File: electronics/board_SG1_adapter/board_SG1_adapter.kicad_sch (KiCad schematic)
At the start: 2 parts

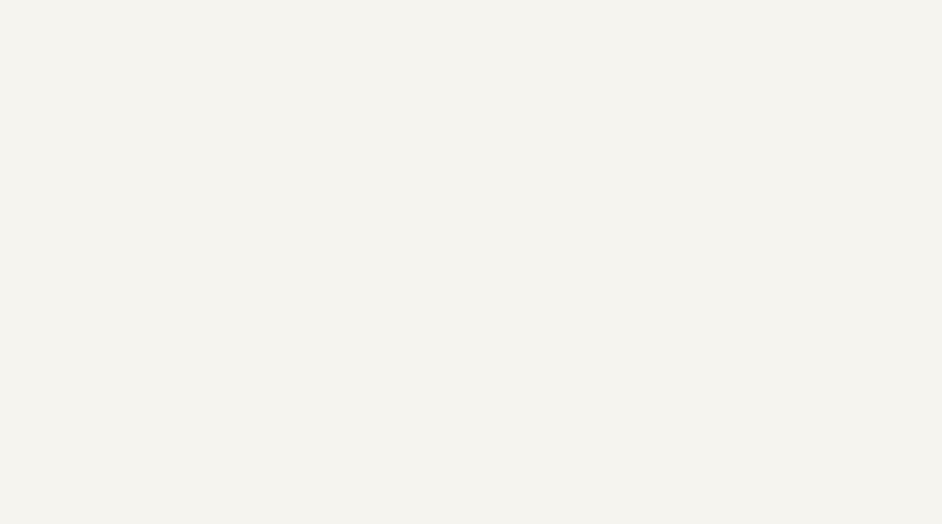
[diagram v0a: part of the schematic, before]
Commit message: WIP schematic entry and component+footprint definitions
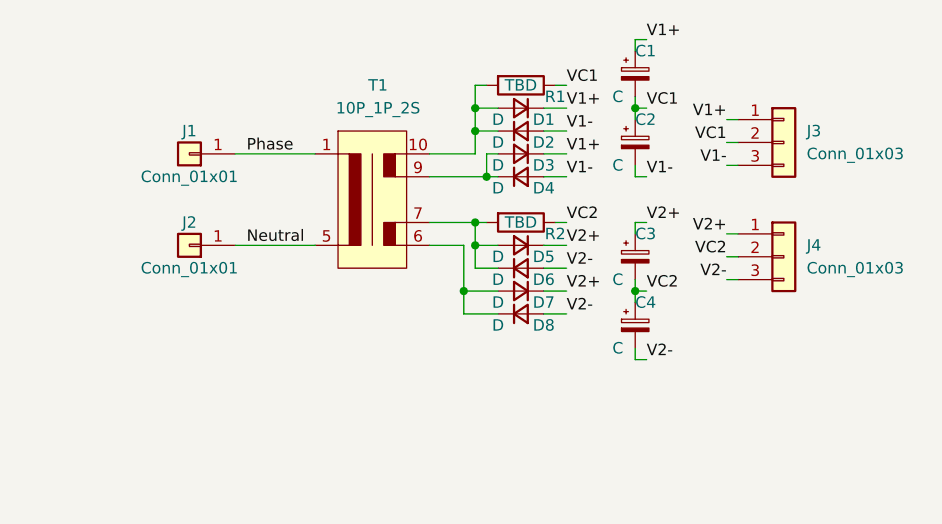
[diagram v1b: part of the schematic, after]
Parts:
- added C1, C2, C3, C4: C, symbol Device:C_Polarized_Small
- added D1, D2, D3, D4, D5, D6, D7, D8: D, Diode_SMD:D_SMA, symbol Device:D_Small
- added J1, J2: Conn_01x01, SquantorConnectors:pad_power, symbol Connector_Generic:Conn_01x01
- added J3, J4: Conn_01x03, symbol Connector_Generic:Conn_01x03
- added R1, R2: TBD, SquantorRcl:R_1206, symbol Device:R
- added T1: 10P_1P_2S, symbol SquantorTransformer:10P_1P_2S
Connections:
- new net: D3.2 (A), D4.1 (K), T1.9
- new net: D5.2 (A), D6.1 (K), R2.2, T1.7
- new net: D1.2 (A), D2.1 (K), R1.2, T1.10
- new net: D7.2 (A), D8.1 (K), T1.6
- new net Neutral: J2.1 (Pin_1), T1.5
- new net Phase: J1.1 (Pin_1), T1.1
- new net V1+: C1.1, D1.1 (K), D3.1 (K), J3.1 (Pin_1)
- new net V1-: C2.2, D2.2 (A), D4.2 (A), J3.3 (Pin_3)
- new net V2+: C3.1, D5.1 (K), D7.1 (K), J4.1 (Pin_1)
- new net V2-: C4.2, D6.2 (A), D8.2 (A), J4.3 (Pin_3)
- new net VC1: C1.2, C2.1, J3.2 (Pin_2), R1.1
- new net VC2: C3.2, C4.1, J4.2 (Pin_2), R2.1

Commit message: WIP rectifier section
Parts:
- added R3, R4: TBD, SquantorRcl:R_1206, symbol Device:R
- D1, D2, D3, D4, D5, D6, D7, D8: footprint Diode_SMD:D_SMA -> Diode_SMD:D_SMB
- T1: footprint (none) -> SquantorTransformer:10pin_5pitch_32x27_1Pri_2Sec
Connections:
- net VC1: now also R2.1
- net VC2: now also R3.1, R4.1; no longer R2.1
- net P1B: now reaches D3.2 (A), D4.1 (K), T1.9
- net P1B: now also R2.2
- net P2A: now reaches D5.2 (A), D6.1 (K), T1.7
- net P2A: now also R3.2; no longer R2.2
- net P1A: now reaches D1.2 (A), D2.1 (K), R1.2, T1.10
- net P2B: now reaches D7.2 (A), D8.1 (K), T1.6
- net P2B: now also R4.2
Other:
- moved on the sheet: D1, D2, D7, D8, R1, R2

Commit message: WIP placing and selecting components
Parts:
- added C5, C6: 100n, SquantorRcl:C_0805+0603, symbol Device:C_Small
- C1, C2, C3, C4: footprint (none) -> SquantorRcl:C-050-075-100-elco
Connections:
- net P2B: now also C5.1, C6.1
- net V2+: now also C5.2
- net V2-: now also C6.2
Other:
- moved on the sheet: D7, D8, R4

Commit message: WIP further development
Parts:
- removed J3, J4: Conn_01x03, symbol Connector_Generic:Conn_01x03
- added C10, C11, C12, C7, C8, C9: 100n, SquantorRcl:C_0805+0603, symbol Device:C_Small
- added C13, C14, C15, C16, C17, C18, C19, C20, C21, C22, C23, C24, C25, C26: 10u, SquantorRcl:C_1206_0805, symbol Device:C_Small
- added J3: Conn_01x06, Connector_Molex:Molex_KK-254_AE-6410-06A_1x06_P2.54mm_Vertical, symbol Connector_Generic:Conn_01x06
- C1, C2, C3, C4: footprint SquantorRcl:C-050-075-100-elco -> SquantorRcl:C-050-100-elco
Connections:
- net P1A: now also C7.1, C8.1
- net P1B: now also C10.1, C9.1
- net P2A: now also C11.1, C12.1
- net V1+: now also C13.1, C17.1, C19.1, C21.1, C23.1, C7.2, C9.2, J3.1 (Pin_1)
- net V1-: now also C10.2, C14.2, C17.2, C19.2, C21.2, C23.2, C8.2, J3.3 (Pin_3)
- net V2+: now also C11.2, C15.1, C18.1, C20.1, C22.1, C24.1, C25.1, J3.4 (Pin_4)
- net V2-: now also C12.2, C16.2, C18.2, C20.2, C22.2, C24.2, C26.2, J3.6 (Pin_6)
- net VC1: now also C13.2, C14.1, J3.2 (Pin_2)
- net VC2: now also C15.2, C16.1, C25.2, C26.1, J3.5 (Pin_5)
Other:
- moved on the sheet: C1, C2, C3, C4, C5, C6, D1, D2, D3, D4, D5, D6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

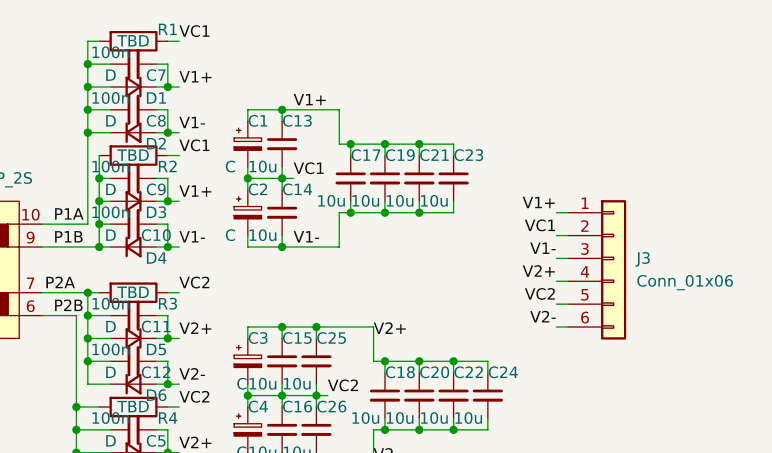
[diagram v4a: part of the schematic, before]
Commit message: routing completed WIP silk placement
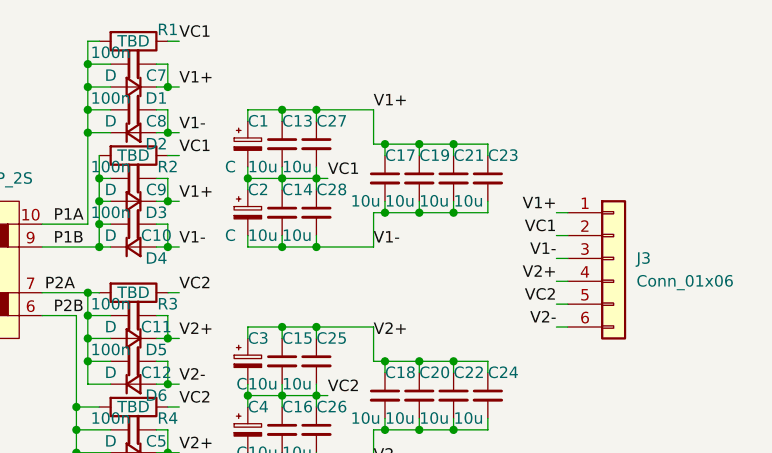
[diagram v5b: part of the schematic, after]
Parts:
- added C27, C28: 10u, SquantorRcl:C_1206_0805, symbol Device:C_Small
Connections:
- net V1+: now also C27.1
- net V1-: now also C28.2
- net VC1: now also C27.2, C28.1
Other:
- moved on the sheet: C17, C19, C21, C23

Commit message: silk placement completed
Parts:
- C1, C2, C3, C4: value C -> 100u
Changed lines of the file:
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@@
       (effects (font (size 1.27 1.27)) (justify left))
     )
-    (property "Value" "C" (id 1) (at 81.28 39.37 0)
+    (property "Value" "100u" (id 1) (at 78.74 39.37 0)
       (effects (font (size 1.27 1.27)) (justify left))
     )
@@
       (effects (font (size 1.27 1.27)) (justify left))
     )
-    (property "Value" "C" (id 1) (at 81.28 31.75 0)
+    (property "Value" "100u" (id 1) (at 78.74 31.75 0)
       (effects (font (size 1.27 1.27)) (justify left))
     )
@@
       (effects (font (size 1.27 1.27)) (justify left))
     )
-    (property "Value" "C" (id 1) (at 82.55 55.88 0)
+    (property "Value" "100u" (id 1) (at 78.74 55.88 0)
       (effects (font (size 1.27 1.27)) (justify left))
     )
@@
       (effects (font (size 1.27 1.27)) (justify left))
     )
-    (property "Value" "C" (id 1) (at 82.55 63.5 0)
+    (property "Value" "100u" (id 1) (at 78.74 63.5 0)
       (effects (font (size 1.27 1.27)) (justify left))
     )
@@
   (symbol_instances
     (path "/33a96a7d-b1b6-4d63-a112-8e0892e19753"
-      (reference "C1") (unit 1) (value "C") (footprint "SquantorRcl:C-050-100-elco")
+      (reference "C1") (unit 1) (value "100u") (footprint "SquantorRcl:C-050-100-elco")
     )
     (path "/2b78c5ce-aeac-4cdf-9dfa-5948914964b5"
-      (reference "C2") (unit 1) (value "C") (footprint "SquantorRcl:C-050-100-elco")
+      (reference "C2") (unit 1) (value "100u") (footprint "SquantorRcl:C-050-100-elco")
     )
     (path "/6118800c-273b-49bc-ae5c-e88a0e55130d"
-      (reference "C3") (unit 1) (value "C") (footprint "SquantorRcl:C-050-100-elco")
+      (reference "C3") (unit 1) (value "100u") (footprint "SquantorRcl:C-050-100-elco")
     )
     (path "/78f42d71-b71d-46fc-9742-f3a159a96a0b"
-      (reference "C4") (unit 1) (value "C") (footprint "SquantorRcl:C-050-100-elco")
+      (reference "C4") (unit 1) (value "100u") (footprint "SquantorRcl:C-050-100-elco")
     )
     (path "/431a0f33-663b-4db5-8d23-d3860d969f31"

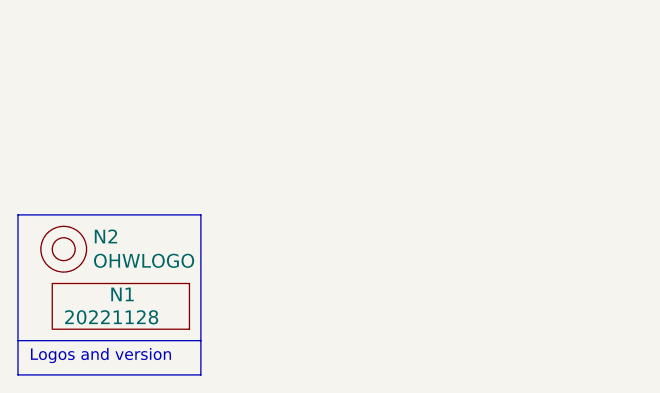
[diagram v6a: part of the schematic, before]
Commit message: added small fixes, through wire holes
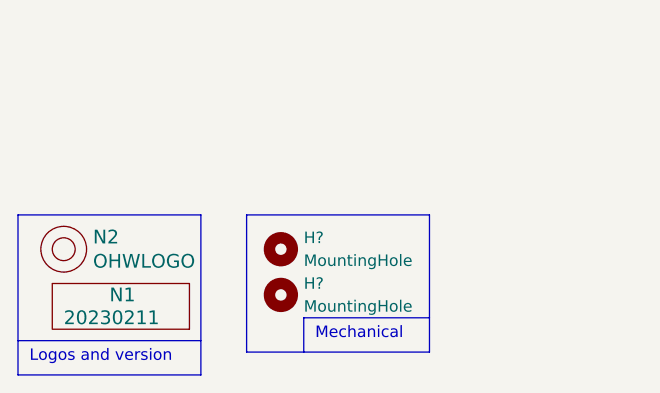
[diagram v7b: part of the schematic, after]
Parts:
- added H? (x2): MountingHole, MountingHole:MountingHole_2.2mm_M2, symbol Mechanical:MountingHole
- N1: value 20221128 -> 20230211
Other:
- note added: "Mechanical"
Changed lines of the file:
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@@
+    (stroke (width 0) (type default) (color 0 0 0 0))
+  )
+  (polyline (pts (xy 60.96 189.23) (xy 46.99 189.23))
     (stroke (width 0) (type default) (color 0 0 0 0))
   )
@@
     (stroke (width 0) (type default) (color 0 0 0 0))
   )
+  (polyline (pts (xy 46.99 189.23) (xy 46.99 193.04))
+    (stroke (width 0) (type default) (color 0 0 0 0))
+  )
   (wire (pts (xy 91.44 39.37) (xy 91.44 40.64))
     (stroke (width 0) (type default) (color 0 0 0 0))
@@
     (stroke (width 0) (type default) (color 0 0 0 0))
   )
+  (polyline (pts (xy 40.64 177.8) (xy 40.64 193.04))
+    (stroke (width 0) (type default) (color 0 0 0 0))
+  )
   (wire (pts (xy 106.68 60.96) (xy 102.87 60.96))
     (stroke (width 0) (type default) (color 0 0 0 0))
@@
     (stroke (width 0) (type default) (color 0 0 0 0))
   )
+  (polyline (pts (xy 60.96 193.04) (xy 60.96 177.8))
+    (stroke (width 0) (type default) (color 0 0 0 0))
+  )
   (wire (pts (xy 110.49 35.56) (xy 110.49 36.83))
     (stroke (width 0) (type default) (color 0 0 0 0))
@@
     (stroke (width 0) (type default) (color 0 0 0 0))
   )
+  (polyline (pts (xy 60.96 177.8) (xy 40.64 177.8))
+    (stroke (width 0) (type default) (color 0 0 0 0))
+  )
   (wire (pts (xy 73.66 20.32) (xy 74.93 20.32))
     (stroke (width 0) (type default) (color 0 0 0 0))
@@
     (stroke (width 0) (type default) (color 0 0 0 0))
   )
+  (polyline (pts (xy 40.64 193.04) (xy 60.96 193.04))
+    (stroke (width 0) (type default) (color 0 0 0 0))
+  )
   (wire (pts (xy 66.04 53.34) (xy 66.04 55.88))
     (stroke (width 0) (type default) (color 0 0 0 0))
@@
   )
   (text "Logos and version" (at 16.51 194.31 0)
+    (effects (font (size 1.27 1.27)) (justify left bottom))
+  )
+  (text "Mechanical" (at 48.26 191.77 0)
     (effects (font (size 1.27 1.27)) (justify left bottom))
   )
@@
       (effects (font (size 1.524 1.524)) (justify left))
     )
-    (property "Value" "20221128" (id 1) (at 20.32 189.23 0)
+    (property "Value" "20230211" (id 1) (at 20.32 189.23 0)
       (effects (font (size 1.524 1.524)) (justify left))
     )
@@
     (pin "2")
   )
+  (symbol (lib_id "Mechanical:MountingHole") (at 44.45 181.61 0) (unit 1)
+    (in_bom yes) (on_board yes) (fields_autoplaced)
+    (property "Reference" "H?" (id 0) (at 46.99 180.3399 0)
+      (effects (font (size 1.27 1.27)) (justify left))
+    )
+    (property "Value" "MountingHole" (id 1) (at 46.99 182.8799 0)
+      (effects (font (size 1.27 1.27)) (justify left))
+    )
+    (property "Footprint" "MountingHole:MountingHole_2.2mm_M2" (id 2) (at 44.45 181.61 0)
+      (effects (font (size 1.27 1.27)) hide)
+    )
+    (property "Datasheet" "~" (id 3) (at 44.45 181.61 0)
+      (effects (font (size 1.27 1.27)) hide)
+    )
+  )
   (symbol (lib_id "Connector_Generic:Conn_01x01") (at 34.29 48.26 180) (unit 1)
     (in_bom yes) (on_board yes)
@@
     (pin "2")
   )
+  (symbol (lib_id "Mechanical:MountingHole") (at 44.45 186.69 0) (unit 1)
+    (in_bom yes) (on_board yes) (fields_autoplaced)
+    (property "Reference" "H?" (id 0) (at 46.99 185.4199 0)
+      (effects (font (size 1.27 1.27)) (justify left))
+    )
+    (property "Value" "MountingHole" (id 1) (at 46.99 187.9599 0)
+      (effects (font (size 1.27 1.27)) (justify left))
+    )
+    (property "Footprint" "MountingHole:MountingHole_2.2mm_M2" (id 2) (at 44.45 186.69 0)
+      (effects (font (size 1.27 1.27)) hide)
+    )
+    (property "Datasheet" "~" (id 3) (at 44.45 186.69 0)
+      (effects (font (size 1.27 1.27)) hide)
+    )
+  )
   (symbol (lib_id "Device:D_Small") (at 71.12 63.5 180) (unit 1)
     (in_bom yes) (on_board yes)
@@
       (reference "D8") (unit 1) (value "D") (footprint "Diode_SMD:D_SMB")
     )
+    (path "/9a78483e-a4a9-442b-9b78-185e6ef8e163"
+      (reference "H?") (unit 1) (value "MountingHole") (footprint "MountingHole:MountingHole_2.2mm_M2")
+    )
+    (path "/c4c5520e-ab64-4797-a9b6-5f1cd79f7616"
+      (reference "H?") (unit 1) (value "MountingHole") (footprint "MountingHole:MountingHole_2.2mm_M2")
+    )
     (path "/79b5ad3e-5f04-49f9-b44e-dfdc53bea2eb"
       (reference "J1") (unit 1) (value "Conn_01x01") (footprint "SquantorConnectors:pad_power")
@@
     )
     (path "/00000000-0000-0000-0000-00005ee12bf3"
-      (reference "N1") (unit 1) (value "20221128") (footprint "SquantorLabels:Label_Generic")
+      (reference "N1") (unit 1) (value "20230211") (footprint "SquantorLabels:Label_Generic")
     )
     (path "/00000000-0000-0000-0000-00005ee13678"

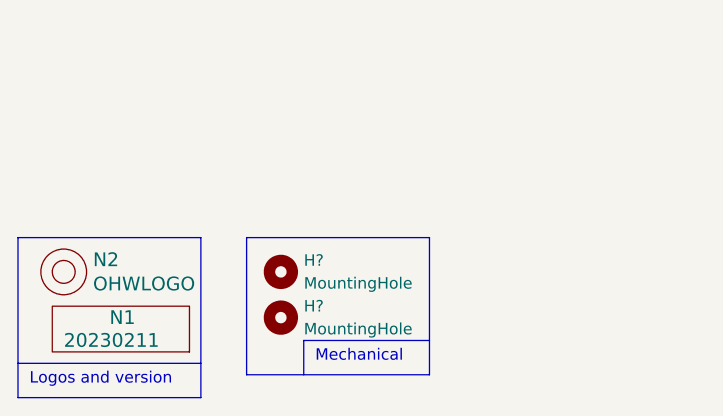
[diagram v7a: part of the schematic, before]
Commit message: added mounting hole definitions (forgot to add
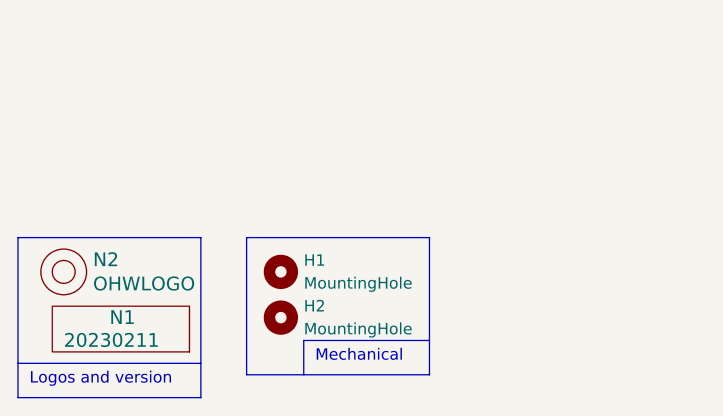
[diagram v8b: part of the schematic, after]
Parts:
- gave numbers to parts that had none: 2
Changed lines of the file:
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@@
   (symbol (lib_id "Mechanical:MountingHole") (at 44.45 181.61 0) (unit 1)
     (in_bom yes) (on_board yes) (fields_autoplaced)
-    (property "Reference" "H?" (id 0) (at 46.99 180.3399 0)
+    (property "Reference" "H1" (id 0) (at 46.99 180.3399 0)
       (effects (font (size 1.27 1.27)) (justify left))
     )
@@
   (symbol (lib_id "Mechanical:MountingHole") (at 44.45 186.69 0) (unit 1)
     (in_bom yes) (on_board yes) (fields_autoplaced)
-    (property "Reference" "H?" (id 0) (at 46.99 185.4199 0)
+    (property "Reference" "H2" (id 0) (at 46.99 185.4199 0)
       (effects (font (size 1.27 1.27)) (justify left))
     )
@@
     )
     (path "/9a78483e-a4a9-442b-9b78-185e6ef8e163"
-      (reference "H?") (unit 1) (value "MountingHole") (footprint "MountingHole:MountingHole_2.2mm_M2")
+      (reference "H1") (unit 1) (value "MountingHole") (footprint "MountingHole:MountingHole_2.2mm_M2")
     )
     (path "/c4c5520e-ab64-4797-a9b6-5f1cd79f7616"
-      (reference "H?") (unit 1) (value "MountingHole") (footprint "MountingHole:MountingHole_2.2mm_M2")
+      (reference "H2") (unit 1) (value "MountingHole") (footprint "MountingHole:MountingHole_2.2mm_M2")
     )
     (path "/79b5ad3e-5f04-49f9-b44e-dfdc53bea2eb"
